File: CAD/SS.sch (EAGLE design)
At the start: 118 parts, among them Q1 SN74AHC-NOR, Q2 UMD5N, Q4 SN74AHC-AND, Q5 BFP460, Q6 TCR1HF50, Q7 NCP553, T1 MMBTRA104SS, X1 ANTENNA, X2 RADIO, X3 INP, X4 AMP-O, X5 BPF-O

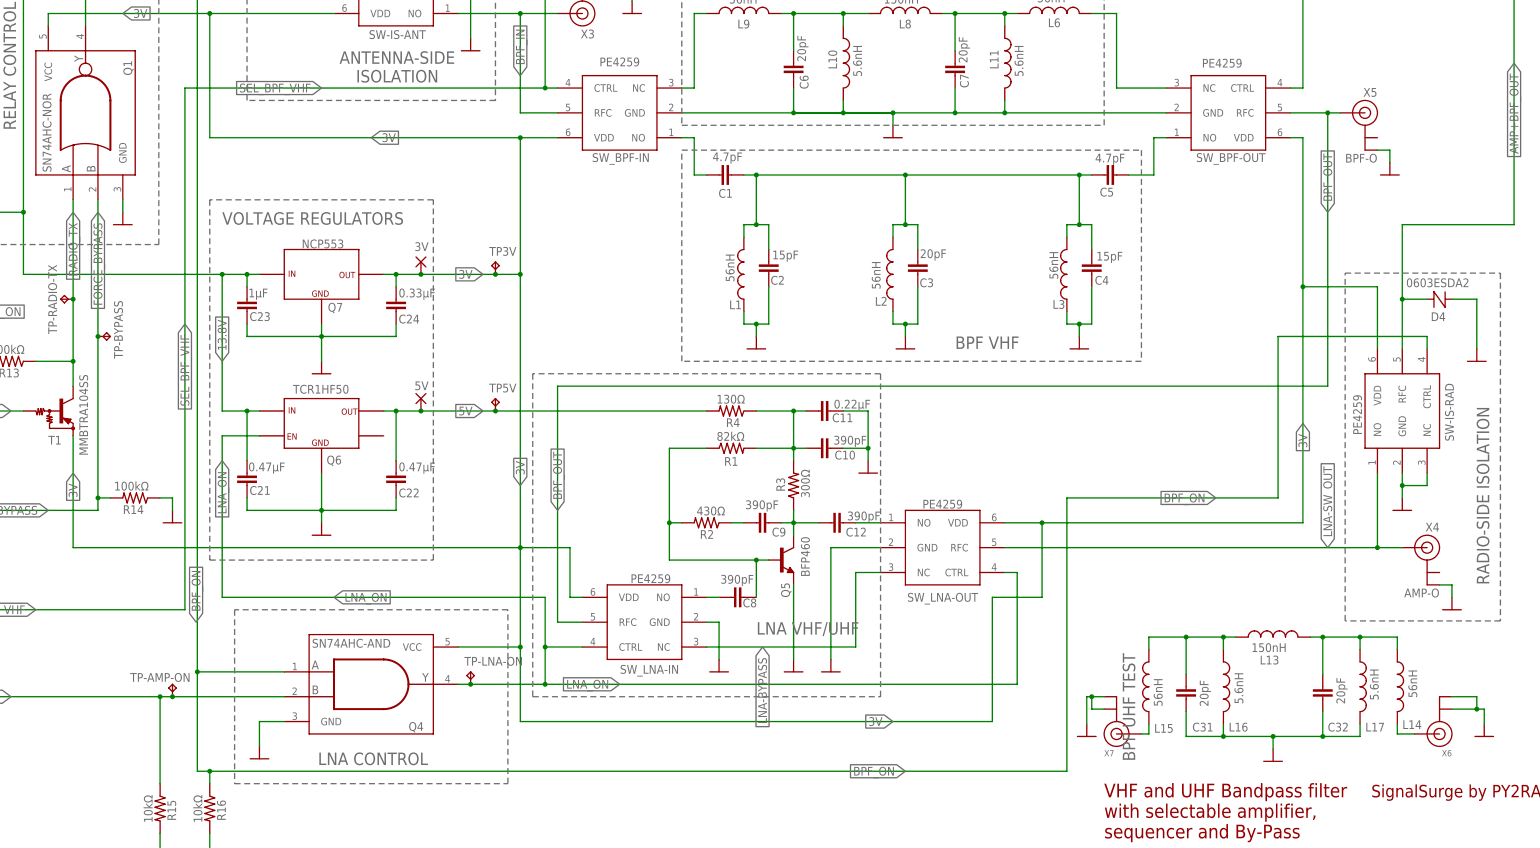
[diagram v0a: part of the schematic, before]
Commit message: Revision D: improvements and corrections
* Added a pulldown resistor in the VHF switch line.
* Refactored the CPW between the relays, hoping this tackle the high
  VSWR found in 70 cm band.
* Removed exposed pads that existed in previous version, that might eff up
  and cause capacitive coupling
* Updated RF testing section
* Updated BOM
* Resolves: #26
* Resolves: #28
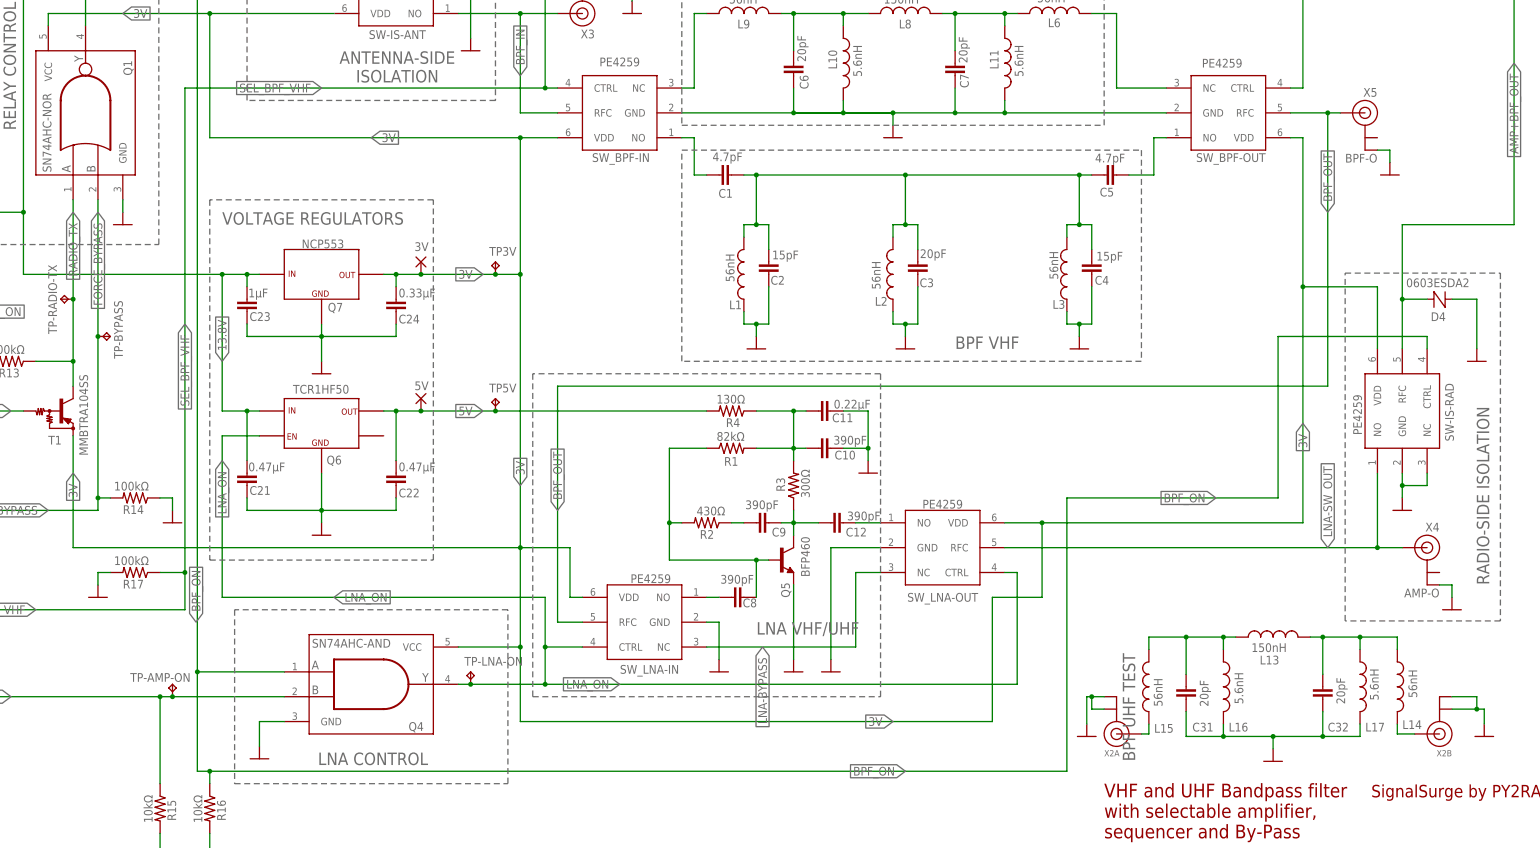
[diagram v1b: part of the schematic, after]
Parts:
- added R17: 100kΩ, aarf:R-1206
- renumbered X6 to X2B, X7 to X2A
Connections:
- net GND: now also R17.2
- net SEL_BPF_VHF: now also R17.1
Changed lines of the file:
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@@
 <part name="L16" library="aarf" deviceset="L-0805" device="" value="5.6nH"/>
 <part name="L17" library="aarf" deviceset="L-0805" device="" value="5.6nH"/>
-<part name="X6" library="adafruit" deviceset="ANTENNA_U.FL" device=""/>
-<part name="X7" library="adafruit" deviceset="ANTENNA_U.FL" device=""/>
+<part name="X2B" library="adafruit" deviceset="ANTENNA_U.FL" device=""/>
+<part name="X2A" library="adafruit" deviceset="ANTENNA_U.FL" device=""/>
 <part name="GND42" library="supply1" library_urn="urn:adsk.eagle:library:371" deviceset="GND" device=""/>
 <part name="GND43" library="supply1" library_urn="urn:adsk.eagle:library:371" deviceset="GND" device=""/>
 <part name="R14" library="aarf" deviceset="R-1206" device="" value="100kΩ"/>
 <part name="GND13" library="supply1" library_urn="urn:adsk.eagle:library:371" deviceset="GND" device=""/>
+<part name="R17" library="aarf" deviceset="R-1206" device="" value="100kΩ"/>
+<part name="GND44" library="supply1" library_urn="urn:adsk.eagle:library:371" deviceset="GND" device=""/>
 </parts>
 <sheets>
@@
 <attribute name="VALUE" x="345.694" y="52.578" size="1.778" layer="96" rot="R90"/>
 </instance>
-<instance part="X6" gate="G$1" x="358.14" y="45.72" smashed="yes" rot="R180">
+<instance part="X2B" gate="G$1" x="358.14" y="45.72" smashed="yes" rot="R180">
 <attribute name="NAME" x="360.68" y="42.418" size="1.27" layer="95" rot="R180"/>
 <attribute name="VALUE" x="360.68" y="55.88" size="1.27" layer="96" rot="R180"/>
 </instance>
-<instance part="X7" gate="G$1" x="292.1" y="45.72" smashed="yes" rot="MR180">
+<instance part="X2A" gate="G$1" x="292.1" y="45.72" smashed="yes" rot="MR180">
 <attribute name="NAME" x="289.56" y="42.418" size="1.27" layer="95" rot="MR180"/>
 <attribute name="VALUE" x="289.56" y="55.88" size="1.27" layer="96" rot="MR180"/>
@@
 </instance>
 <instance part="GND13" gate="1" x="99.06" y="88.9" smashed="yes"/>
+<instance part="R17" gate="G$1" x="91.44" y="78.74" smashed="yes" rot="R180">
+<attribute name="NAME" x="93.218" y="77.2414" size="1.778" layer="95" rot="R180"/>
+<attribute name="VALUE" x="94.234" y="82.042" size="1.778" layer="96" rot="R180"/>
+</instance>
+<instance part="GND44" gate="1" x="83.82" y="73.66" smashed="yes"/>
 </instances>
 <busses>
@@
 <pinref part="FB5" gate="G$1" pin="2"/>
 <wire x1="101.6" y1="71.12" x2="48.26" y2="71.12" width="0.1524" layer="91"/>
-<wire x1="101.6" y1="177.8" x2="101.6" y2="71.12" width="0.1524" layer="91"/>
+<wire x1="101.6" y1="177.8" x2="101.6" y2="78.74" width="0.1524" layer="91"/>
 <label x="101.6" y="129.54" size="1.778" layer="95" rot="R270" xref="yes"/>
 <label x="71.12" y="71.12" size="1.778" layer="95" rot="R180" xref="yes"/>
 <pinref part="TP-VHF-ON" gate="G$1" pin="TP"/>
+<wire x1="101.6" y1="78.74" x2="101.6" y2="71.12" width="0.1524" layer="91"/>
 <wire x1="231.14" y1="208.28" x2="231.14" y2="205.74" width="0.1524" layer="91"/>
 <junction x="231.14" y="205.74"/>
+<pinref part="R17" gate="G$1" pin="1"/>
+<wire x1="101.6" y1="78.74" x2="96.52" y2="78.74" width="0.1524" layer="91"/>
+<junction x="101.6" y="78.74"/>
 </segment>
 </net>
@@
 </segment>
 <segment>
-<pinref part="X7" gate="G$1" pin="GND@1"/>
+<pinref part="X2A" gate="G$1" pin="GND@1"/>
 <pinref part="GND43" gate="1" pin="GND"/>
 <wire x1="289.56" y1="53.34" x2="287.02" y2="53.34" width="0.1524" layer="91"/>
 <wire x1="287.02" y1="53.34" x2="286.004" y2="53.34" width="0.1524" layer="91"/>
 <wire x1="286.004" y1="53.34" x2="286.004" y2="47.752" width="0.1524" layer="91"/>
-<pinref part="X7" gate="G$1" pin="GND@0"/>
+<pinref part="X2A" gate="G$1" pin="GND@0"/>
 <wire x1="289.56" y1="50.8" x2="287.02" y2="50.8" width="0.1524" layer="91"/>
 <wire x1="287.02" y1="50.8" x2="287.02" y2="53.34" width="0.1524" layer="91"/>
@@
 </segment>
 <segment>
-<pinref part="X6" gate="G$1" pin="GND@0"/>
+<pinref part="X2B" gate="G$1" pin="GND@0"/>
 <pinref part="GND42" gate="1" pin="GND"/>
 <wire x1="360.68" y1="50.8" x2="365.76" y2="50.8" width="0.1524" layer="91"/>
 <wire x1="365.76" y1="50.8" x2="367.284" y2="50.8" width="0.1524" layer="91"/>
 <wire x1="367.284" y1="50.8" x2="367.284" y2="47.752" width="0.1524" layer="91"/>
-<pinref part="X6" gate="G$1" pin="GND@1"/>
+<pinref part="X2B" gate="G$1" pin="GND@1"/>
 <wire x1="360.68" y1="53.34" x2="365.76" y2="53.34" width="0.1524" layer="91"/>
 <wire x1="365.76" y1="53.34" x2="365.76" y2="50.8" width="0.1524" layer="91"/>
@@
 <wire x1="96.52" y1="93.98" x2="99.06" y2="93.98" width="0.1524" layer="91"/>
 <wire x1="99.06" y1="93.98" x2="99.06" y2="91.44" width="0.1524" layer="91"/>
+</segment>
+<segment>
+<pinref part="R17" gate="G$1" pin="2"/>
+<wire x1="86.36" y1="78.74" x2="83.82" y2="78.74" width="0.1524" layer="91"/>
+<pinref part="GND44" gate="1" pin="GND"/>
+<wire x1="83.82" y1="78.74" x2="83.82" y2="76.2" width="0.1524" layer="91"/>
 </segment>
 </net>
@@
 <net name="N$2" class="0">
 <segment>
-<pinref part="X7" gate="G$1" pin="SIGNAL"/>
+<pinref part="X2A" gate="G$1" pin="SIGNAL"/>
 <pinref part="L15" gate="G$1" pin="1"/>
 <wire x1="297.18" y1="45.72" x2="298.704" y2="45.72" width="0.1524" layer="91"/>
@@
 <net name="N$12" class="0">
 <segment>
-<pinref part="X6" gate="G$1" pin="SIGNAL"/>
+<pinref part="X2B" gate="G$1" pin="SIGNAL"/>
 <wire x1="353.06" y1="45.72" x2="349.504" y2="45.72" width="0.1524" layer="91"/>
 <pinref part="L14" gate="G$1" pin="2"/>

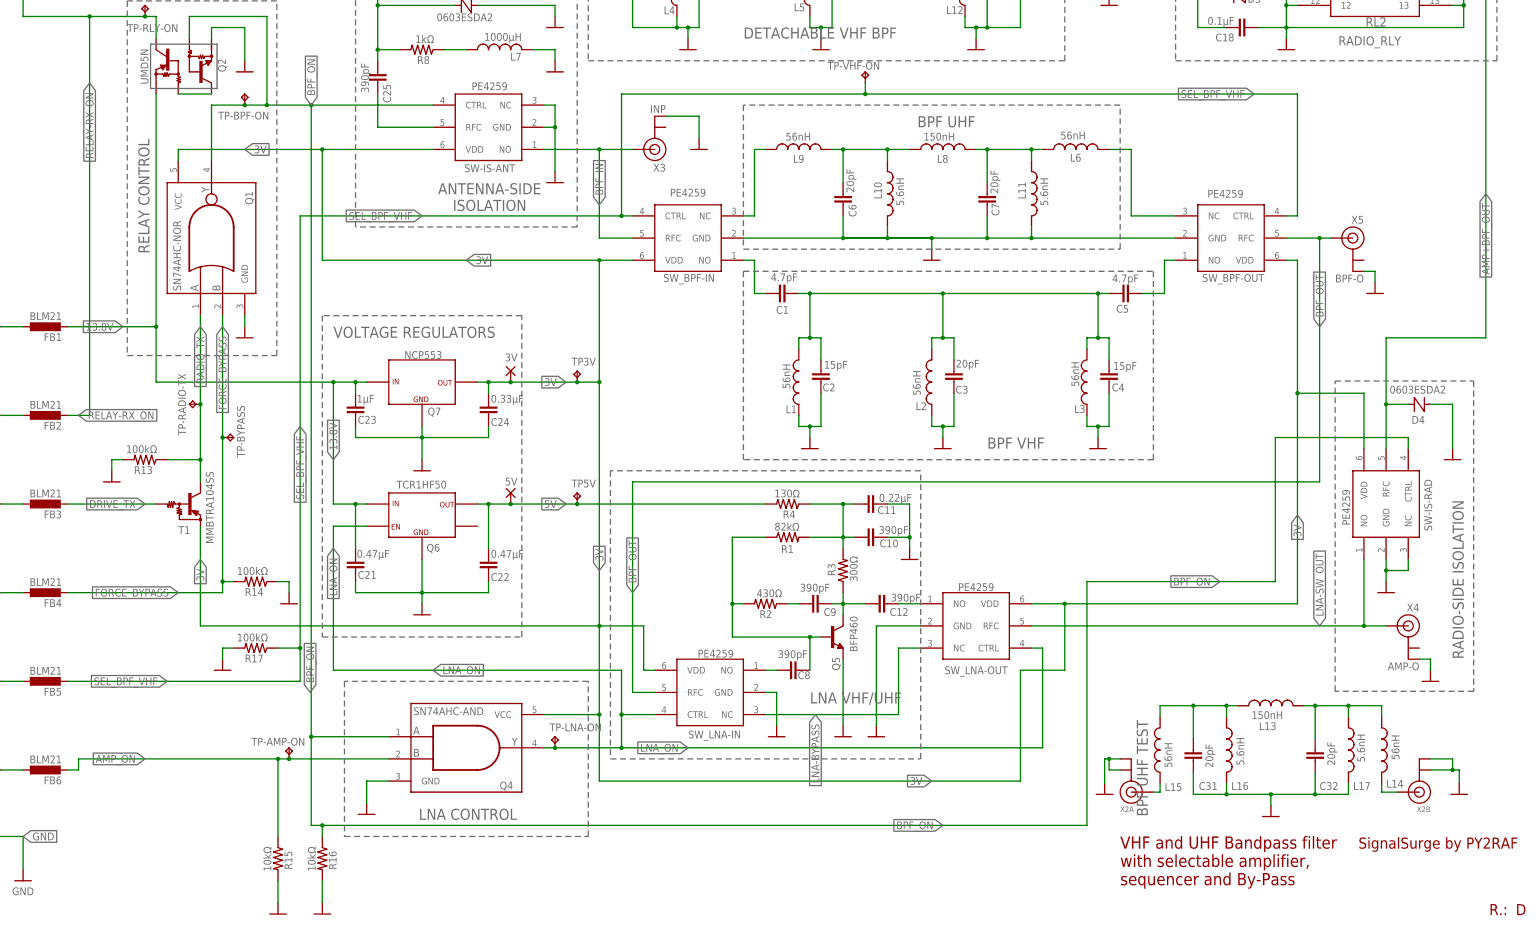
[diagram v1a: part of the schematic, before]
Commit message: Removed two RF switches
Removed two unneeded RF switches at the front-end: extra cost,
complexity and insertion loss - unnecessarily, as the RF stage
is handsomely isolated - and powered off during high power operations.
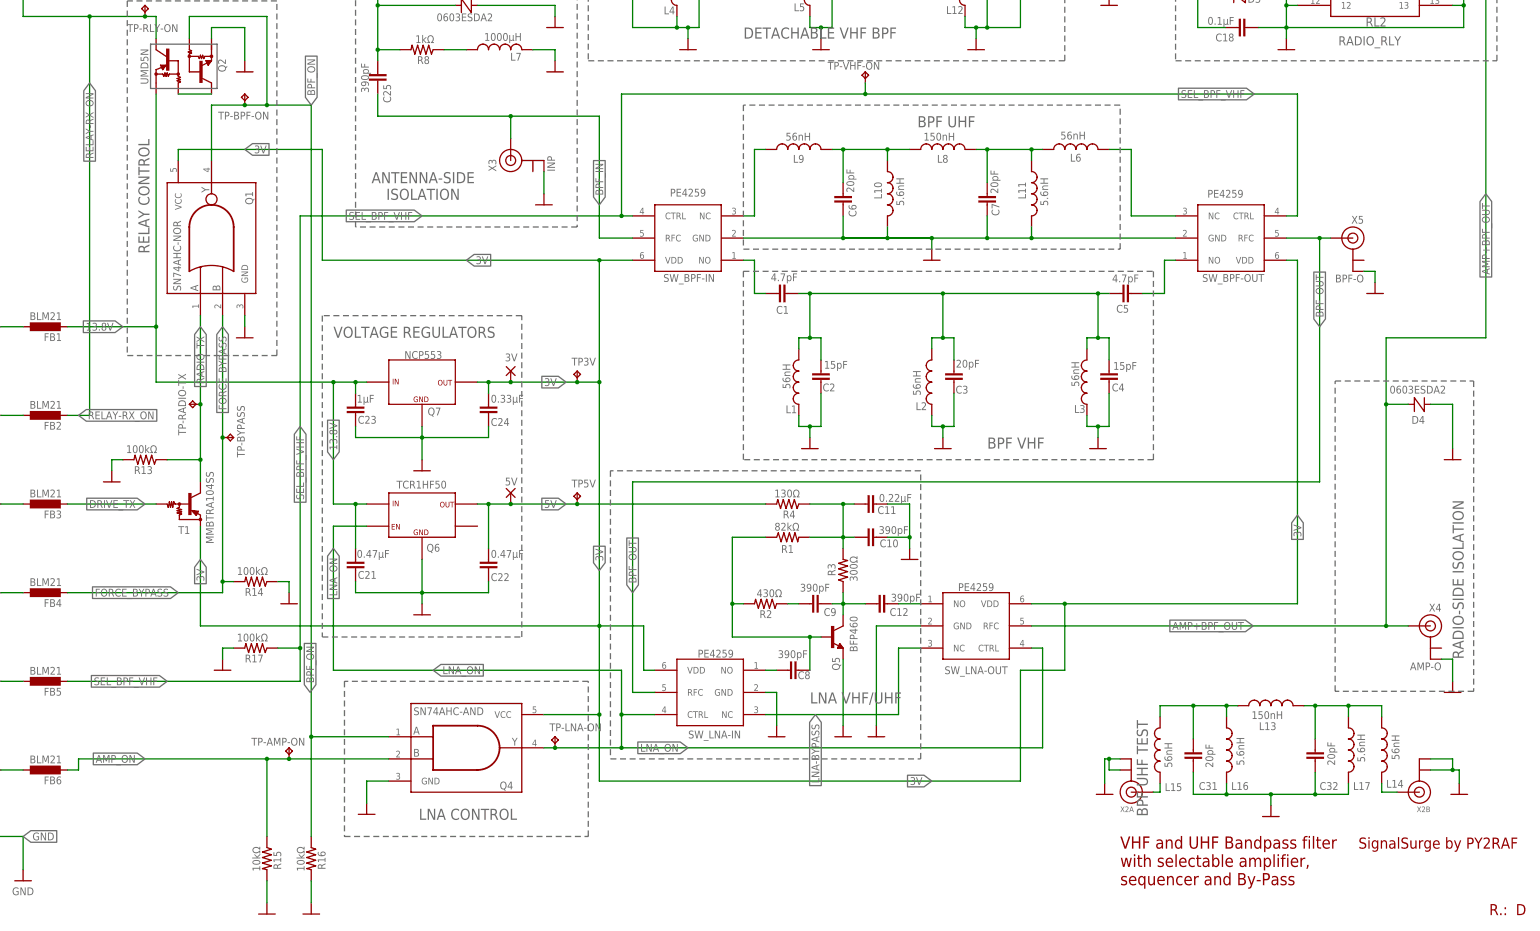
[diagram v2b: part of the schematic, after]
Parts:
- removed SW-IS-ANT, SW-IS-RAD: PE4259, aarf:PE4259
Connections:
- removed net LNA-SW_OUT: SW-IS-RAD.NO, SW_LNA-OUT.RFC, X4.SIGNAL
- removed net N$17: C25.1, SW-IS-ANT.RFC
- net 3V: no longer SW-IS-ANT.VDD, SW-IS-RAD.VDD
- net AMP+BPF_OUT: now also SW_LNA-OUT.RFC, X4.SIGNAL; no longer SW-IS-RAD.RFC
- net BPF_IN: now also C25.1; no longer SW-IS-ANT.NO
- net BPF_ON: no longer SW-IS-ANT.CTRL, SW-IS-RAD.CTRL
- net GND: no longer SW-IS-ANT.GND, SW-IS-ANT.NC, SW-IS-RAD.GND, SW-IS-RAD.NC
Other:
- moved on the sheet: R15, R16, X3, X4

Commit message: Launching: Rev. E
* Complete rewrite of VHF BPF to a proper 3-pole ¤
* Improved UHF filter performance significantly¤
* Implemented a proper 50 ohm GCPW setup ¤
* Re-added soldermask into the signal path ¤
* Added a two-pole and three-pole test pad at the back of the board
* Fixed u.FL connectors lacking connection to ground in one side
* Added keep-out zones for RF inductors ¤
* Replaced the 3V regulator with one that can withstand the Vin ¤
* Separated the top ground plane on north/south: The north (RF) section
  doesn't have any thermal relief in GND pads. The south (ancillary)
  section contains thermal relief GND pads. ¤
* Fixed wrong limiters & pulldowns across the board ¤

All issues marked with ¤ were suggested by Gemini AI.
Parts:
- removed Q7: NCP553, aarf:NCP553
- removed R11, R16: 10kΩ, aarf:R-1206
- added C33, C35: 4.7pF, aarf:C-0805
- added C34, C36, C37, C38, C39: 1.5pF, aarf:C-0805
- added C40: Cin, aarf:C-0805
- added C41: Ct1, aarf:C-0805
- added C42: Cc1, aarf:C-0805
- added C43: Ct2, aarf:C-0805
- added C44: Cc2, aarf:C-0805
- added C45: Ct3, aarf:C-0805
- added C46: Cout, aarf:C-0805
- added Q3: MIC5205, aarf:MIC5205
- added X3A, X3B: (no value), adafruit:ANTENNA_U.FL
- C23: value 1µF -> 470pF
- C24: value 0.33µF -> 2.2µF
- C28, C3: value 20pF -> 18pF
- C31: value 20pF -> Ct1
- C32: value 20pF -> Ct2
- C6, C7: value 20pF -> 8.2pF
- L10, L11: value 5.6nH -> 8.2nH
- L13: value 150nH -> Cc; device aarf:L-0805 -> aarf:C-0805
- L14: value 56nH -> Cout; device aarf:L-0805 -> aarf:C-0805
- L15: value 56nH -> Cin; device aarf:L-0805 -> aarf:C-0805
- L16: value 5.6nH -> L1
- L17: value 5.6nH -> L2
- L6: value 56nH -> Lt1
- L8: value 150nH -> Lt2
- L9: value 56nH -> Lt3
- R12, R7: value 10kΩ -> 1kΩ
- R13, R14, R17: value 100kΩ -> 10kΩ
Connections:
- net N$10 renamed T-V-P1
- net N$12 renamed T-V-IN
- net N$2 renamed T-V-OUT
- net N$5 renamed D-V-OUT
- net N$6 renamed D-V-IN
- net N$9 renamed T-V-P2
- removed net BPF_VHF: C1.1, C2.1, C3.1, C4.1, C5.1, L1.2, L2.2, L3.1
- removed net N$11: C7.2, L11.1, L6.1, L8.2
- removed net N$42: FB5.1, R11.1
- removed net N$8: C6.2, L10.1, L8.1, L9.2
- new net D-V-P1: C26.1, C27.1, C38.2, L4.2
- new net D-V-P2: C28.1, C38.1, C39.2, L5.2
- new net D-V-P3: C29.1, C30.1, C39.1, L12.1
- new net T-U-IN: C40.1, X3A.SIGNAL
- new net T-U-OUT: C46.1, X3B.SIGNAL
- new net T-U-P1: C40.2, C41.1, C42.1, L6.1
- new net T-U-P2: C42.2, C43.1, C44.1, L8.1
- new net T-U-P3: C44.2, C45.1, C46.2, L9.1
- new net UHF-P1: C33.2, C34.1, C6.2, L10.1
- new net UHF-P2: C34.2, C35.1, C7.2, L11.1
- new net VHF-P1: C1.1, C2.1, C36.2, L1.2
- new net VHF-P3: C37.1, C4.1, C5.1, L3.1
- new net VPF-P2: C3.1, C36.1, C37.2, L2.2
- net 13.8V: now also Q3.EN, Q3.VIN; no longer C23.2, Q7.IN
- net 3V: now also Q3.VOUT; no longer Q7.OUT
- net AMP+BPF_OUT: now also D4.A; no longer D4.C
- net BPF_ON: no longer R16.1
- net GND: now also C41.2, C43.2, C45.2, D4.C, L6.2, L8.2, L9.2, Q3.GND, X3.GND@0, X3A.GND@0, X3A.GND@1, X3B.GND@0, X3B.GND@1, X4.GND@0, X5.GND@0; no longer D4.A, Q7.GN, R16.2
- net N$4: now also C23.2, Q3.ADJ-BYP; no longer C26.1, C27.1, C28.1, C29.1, C30.1, L12.1, L4.2, L5.2
- net UHF-IN: now also C33.1; no longer L9.1
- net UHF-OUT: now also C35.2; no longer L6.2
- net VHF_ON_IN: now also FB5.1; no longer R11.2
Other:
- note added: "THREE-POLE TEST FILTER"
- note added: "TWO-POLE TEST FILTER"
- note removed: "BPF UHF TEST"
- note removed: "RADIO-SIDE ISOLATION"
- moved on the sheet: 3V, C23, C24, D4
